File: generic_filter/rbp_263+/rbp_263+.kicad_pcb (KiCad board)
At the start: 2 copper layers, 74.4 x 76.4 mm, 63 parts, among them J1 RF_IN, J10 +5V, J11 RF_OUT, J12 RF_OUT, J13 +5V, J14 VSHUT, J2 RF_OUT, J3 RF_IN, J4 RF_OUT, J5 RF_IN, J6 RF_OUT, J7 RF_IN, J8 RF_IN, J9 +5V, U1 RBP263+/RBP188+, U3 PHA-13LN

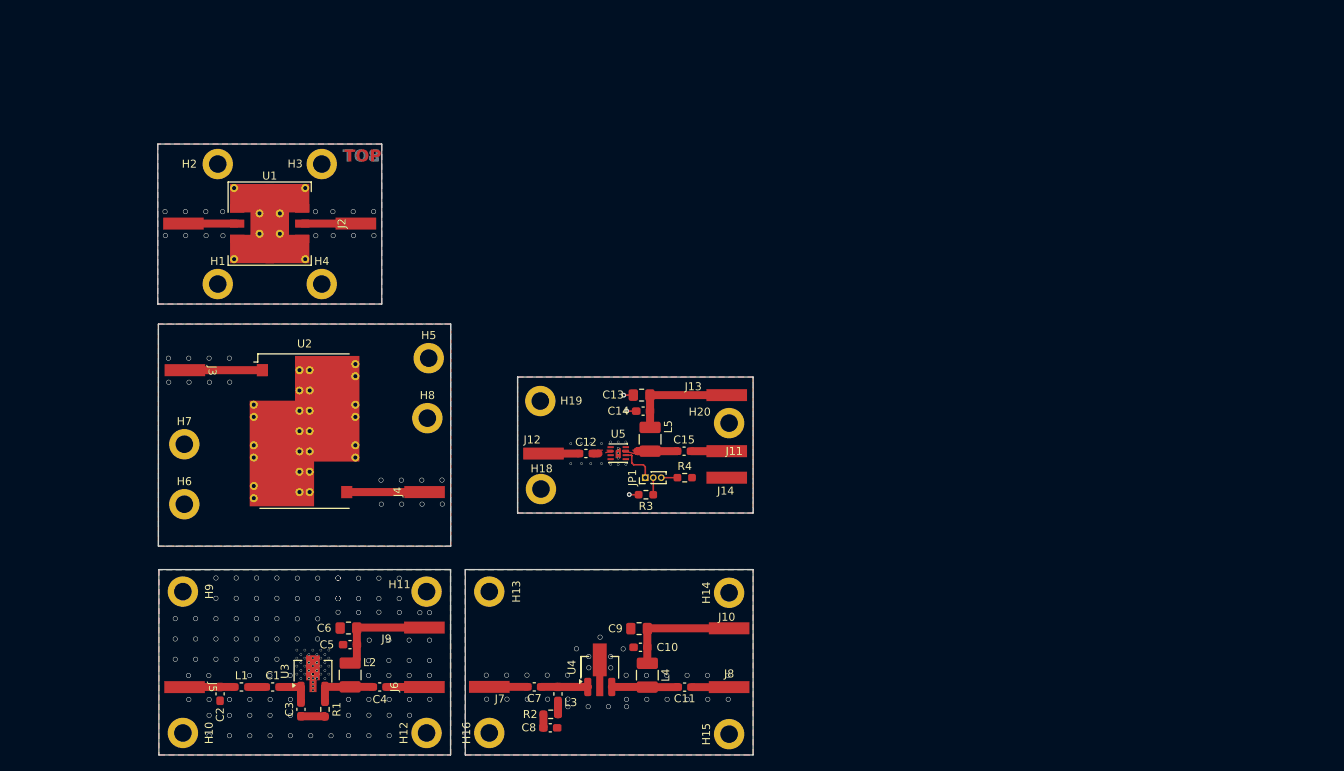
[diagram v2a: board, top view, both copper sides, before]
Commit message: added gdt, tvs schematics and footprints
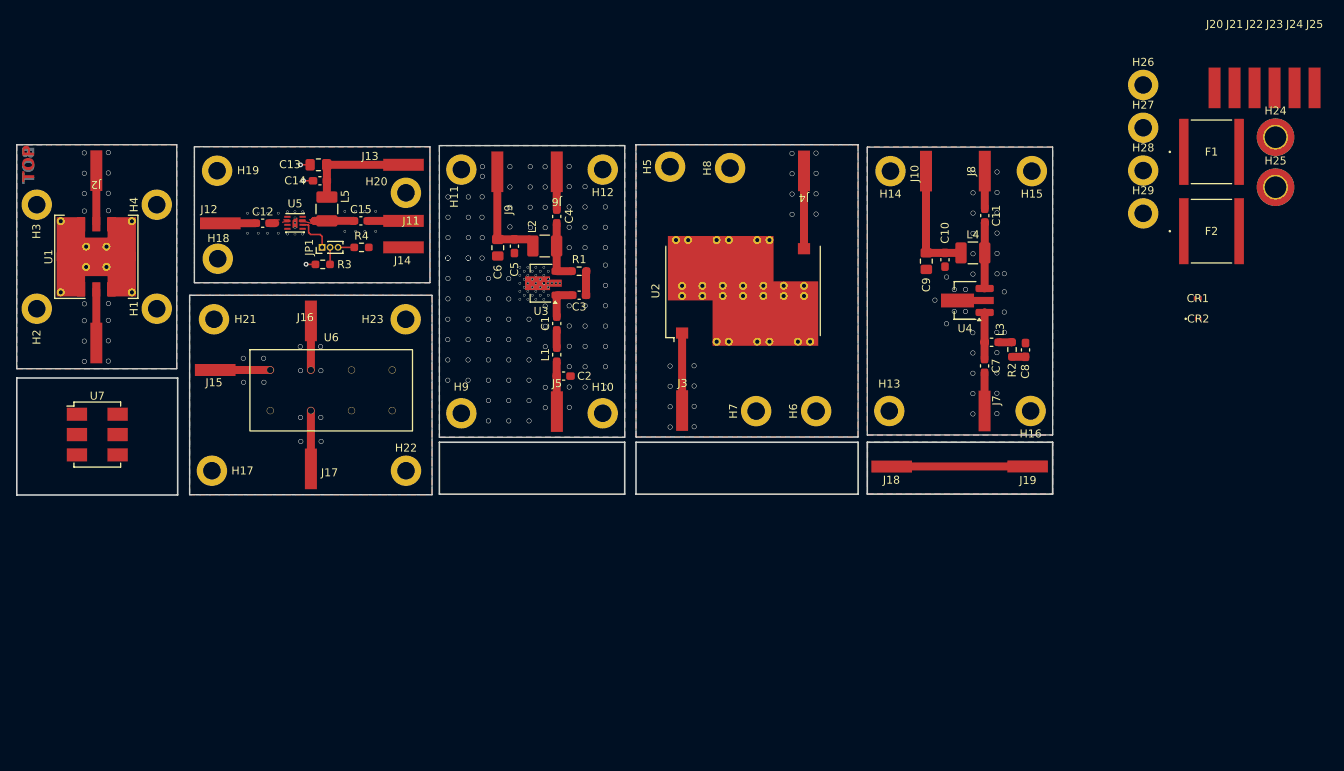
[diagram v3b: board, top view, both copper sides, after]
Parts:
- added CR1: SP3021-01ETG, SP3021:SOD882_LTF, F.Cu at (240.1, 83.2)
- added CR2: SP3031-01ETG, SP3031:SOD882_LTF-L, F.Cu at (240.2, 85.8)
- added F1: 2029-09-SM-RPLF, 2029-09-SMLF:FUSE_2029-09-SM-RPLF_BRN, F.Cu at (241.8, 64.9)
- added F2: 2029-09-SM-RPLF, 2029-09-SMLF:FUSE_2029-09-SM-RPLF_BRN, F.Cu at (241.8, 74.8)
- added H17: MountingHole_Pad, MountingHole:MountingHole_2.2mm_M2_DIN965_Pad, F.Cu at (116.9, 104.7)
- added H21: MountingHole_Pad, MountingHole:MountingHole_2.2mm_M2_DIN965_Pad, F.Cu at (117.2, 85.8)
- added H22: MountingHole_Pad, MountingHole:MountingHole_2.2mm_M2_DIN965_Pad, F.Cu at (141.2, 104.7)
- added H23: MountingHole_Pad, MountingHole:MountingHole_2.2mm_M2_DIN965_Pad, F.Cu at (141.1, 85.8)
- added H24: MountingHole_Pad, MountingHole:MountingHole_2.7mm_M2.5_DIN965_Pad_TopBottom, F.Cu at (249.8, 63.0)
- added H25: MountingHole_Pad, MountingHole:MountingHole_2.7mm_M2.5_DIN965_Pad_TopBottom, F.Cu at (249.8, 69.3)
- added H26: MountingHole_Pad, MountingHole:MountingHole_2.2mm_M2_DIN965_Pad, F.Cu at (233.3, 56.5)
- added H27: MountingHole_Pad, MountingHole:MountingHole_2.2mm_M2_DIN965_Pad, F.Cu at (233.3, 61.9)
- added H28: MountingHole_Pad, MountingHole:MountingHole_2.2mm_M2_DIN965_Pad, F.Cu at (233.3, 67.2)
- added H29: MountingHole_Pad, MountingHole:MountingHole_2.2mm_M2_DIN965_Pad, F.Cu at (233.3, 72.6)
- added J15: RF_IN, PanelMountRF_DC:RF_SMA_Edge_PanelMount, F.Cu at (117.1, 92.1)
- added J16: CPL, PanelMountRF_DC:RF_SMA_Edge_PanelMount, F.Cu at (131.0, 85.6)
- added J17: OUTP, PanelMountRF_DC:RF_SMA_Edge_PanelMount, F.Cu at (129.3, 104.9)
- added J18: RF_IN, PanelMountRF_DC:RF_SMA_Edge_PanelMount, F.Cu at (201.9, 104.2)
- added J19: OUTP, PanelMountRF_DC:RF_SMA_Edge_PanelMount, F.Cu at (218.8, 104.2)
- added J20: RF_IN, PanelMountRF_DC:RF_SMA_Edge_PanelMount, F.Cu at (242.2, 56.9)
- added J21: OUTP, PanelMountRF_DC:RF_SMA_Edge_PanelMount, F.Cu at (244.7, 56.9)
- added J22: PORT_1, PanelMountRF_DC:RF_SMA_Edge_PanelMount, F.Cu at (247.2, 56.9)
- added J23: PORT_2, PanelMountRF_DC:RF_SMA_Edge_PanelMount, F.Cu at (249.7, 56.9)
- added J24: PORT_J, PanelMountRF_DC:RF_SMA_Edge_PanelMount, F.Cu at (252.2, 56.9)
- added J25: PORT_S, PanelMountRF_DC:RF_SMA_Edge_PanelMount, F.Cu at (254.7, 56.9)
- added U6: PDC-15-6+, minickts_kicad:Mini-Circuits_A01, F.Cu at (131.8, 94.7)
- added U7: ~, minickts_kicad:Mini-Circuits_CD636_H4.11mm, F.Cu at (102.6, 100.2)
- J12: value RF_OUT -> RF_IN
- moved H15 79.9 mm to (219.4, 67.3), turned to 180 degrees
- moved H6 79.8 mm to (192.4, 97.3), turned to 90 degrees
- moved H16 78.7 mm to (219.2, 97.3), turned to 180 degrees
- moved C8 75.9 mm to (218.6, 89.6), turned to -90 degrees
- moved H12 73.8 mm to (165.7, 67.1), turned to 180 degrees
- moved R2 73.5 mm to (216.9, 89.6), turned to 90 degrees
- moved J8 72.0 mm to (213.5, 67.3), turned to 180 degrees
- moved H7 71.6 mm to (184.9, 97.3), turned to 90 degrees
- moved J7 70.4 mm to (213.5, 96.0), turned to 180 degrees
- moved C11 69.9 mm to (213.5, 72.9), turned to -90 degrees
- moved L3 69.8 mm to (214.3, 88.7), turned to 0 degrees
- moved C7 69.1 mm to (213.5, 91.6), turned to -90 degrees
- moved L4 66.7 mm to (212.0, 77.5), turned to 0 degrees
- moved J6 66.5 mm to (160.0, 67.4), turned to 180 degrees
- moved H10 66.0 mm to (165.7, 97.6), turned to 180 degrees
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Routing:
- net Net-(J18-Pin_1): track 0.00 -> 17.0 mm
- net Net-(J17-Pin_1): track 0.00 -> 7.28 mm
- net Net-(J15-Pin_1): track 0.00 -> 6.88 mm
- net Net-(J16-Pin_1): track 0.00 -> 6.14 mm
- net GND: vias 224 -> 244
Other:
- board size 74.4 x 76.4 mm -> 129.5 x 43.8 mm
